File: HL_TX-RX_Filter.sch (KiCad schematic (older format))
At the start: 186 parts, among them J1 To Antenna, J2 From Tx, J3 ICSP, J4 Data In, J5 SCL SDA, J6 To Rx in, Q1 2N7002, Q2 2N7002, Q3 2N7002, Q4 2N7002, Q5 2N7002, Q6 2N7002, Q7 2N7002, Q8 2N7002, U1 LD1117S33TR, U10 PE4259, U11 PE4259, U12 PE4259, U13 PE4259, U2 ATMEGA328-AU, U3 PE4259, U4 PE4259, U5 PE4259, U6 PE4259, U7 PE4259, U8 PE4259, U9 PE4259

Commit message: Further progress on layout
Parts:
- added C69, C70, C71, C72: .1u, Capacitors_SMD:C_1206_HandSoldering, symbol C
- added J10: CNR4, Connectors:1pin, symbol TEST_1P
- added J7: CNR1, Connectors:1pin, symbol TEST_1P
- added J8: CNR3, Connectors:1pin, symbol TEST_1P
- added J9: CNR2, Connectors:1pin, symbol TEST_1P
- D13, D14: footprint Diodes_SMD:MELF_Handsoldering -> Diodes_SMD:D_MiniMELF_Handsoldering
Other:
- moved on the sheet: L11, L12, L13, L14

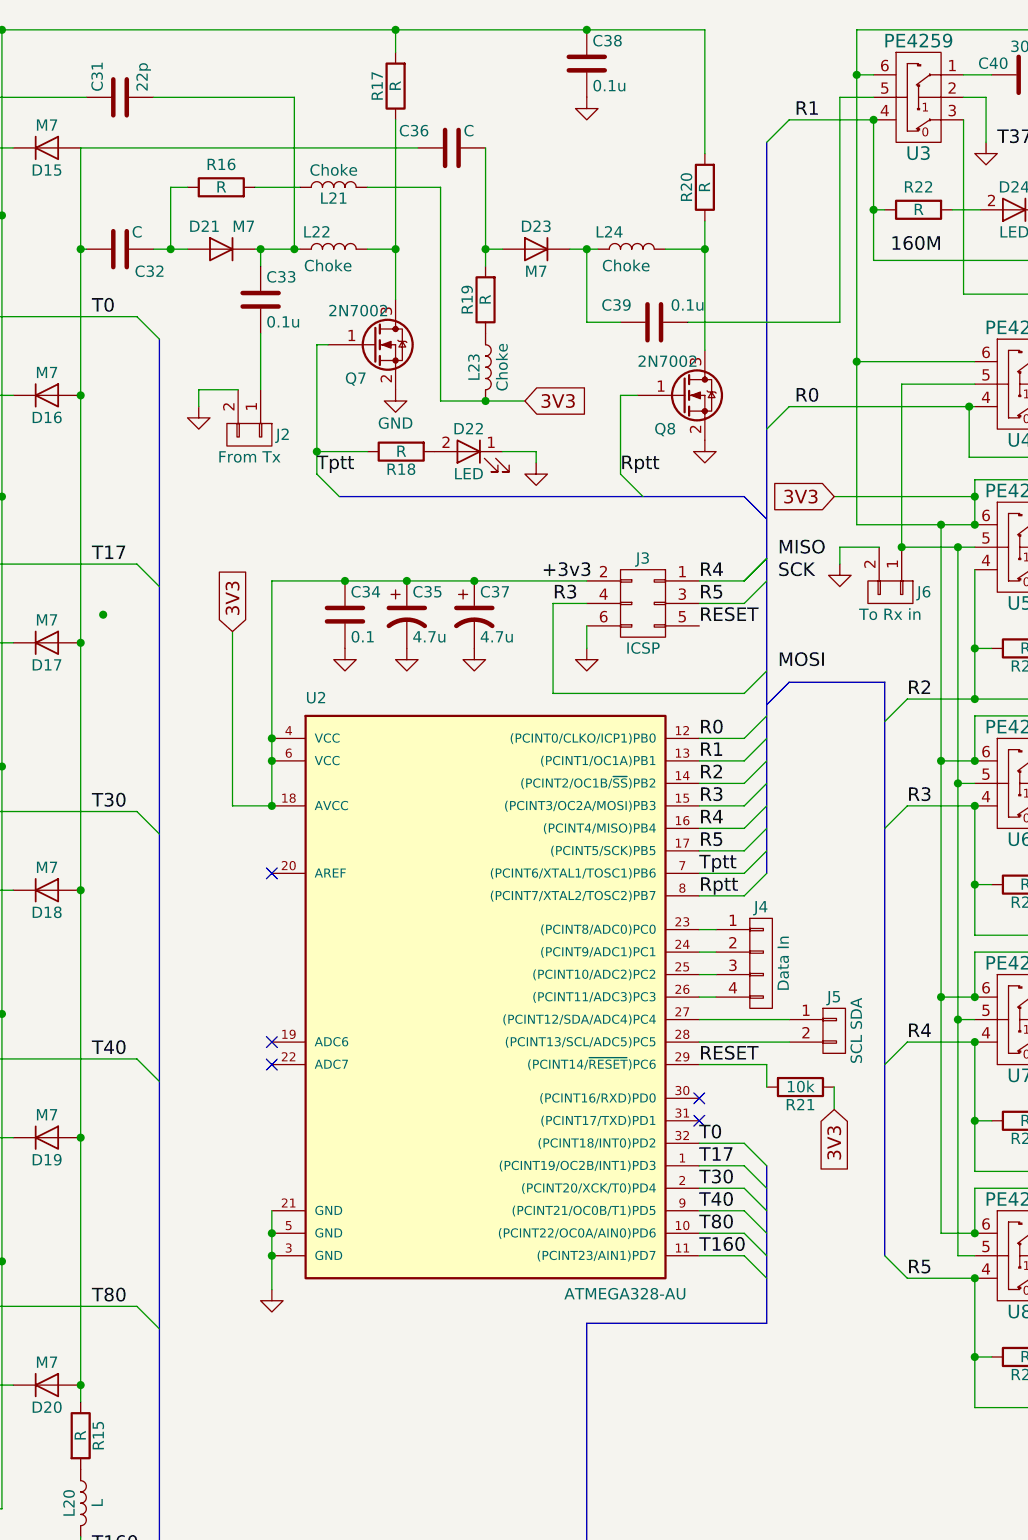
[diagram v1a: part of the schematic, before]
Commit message: Rearranging pins on microprocessor to better fit layout
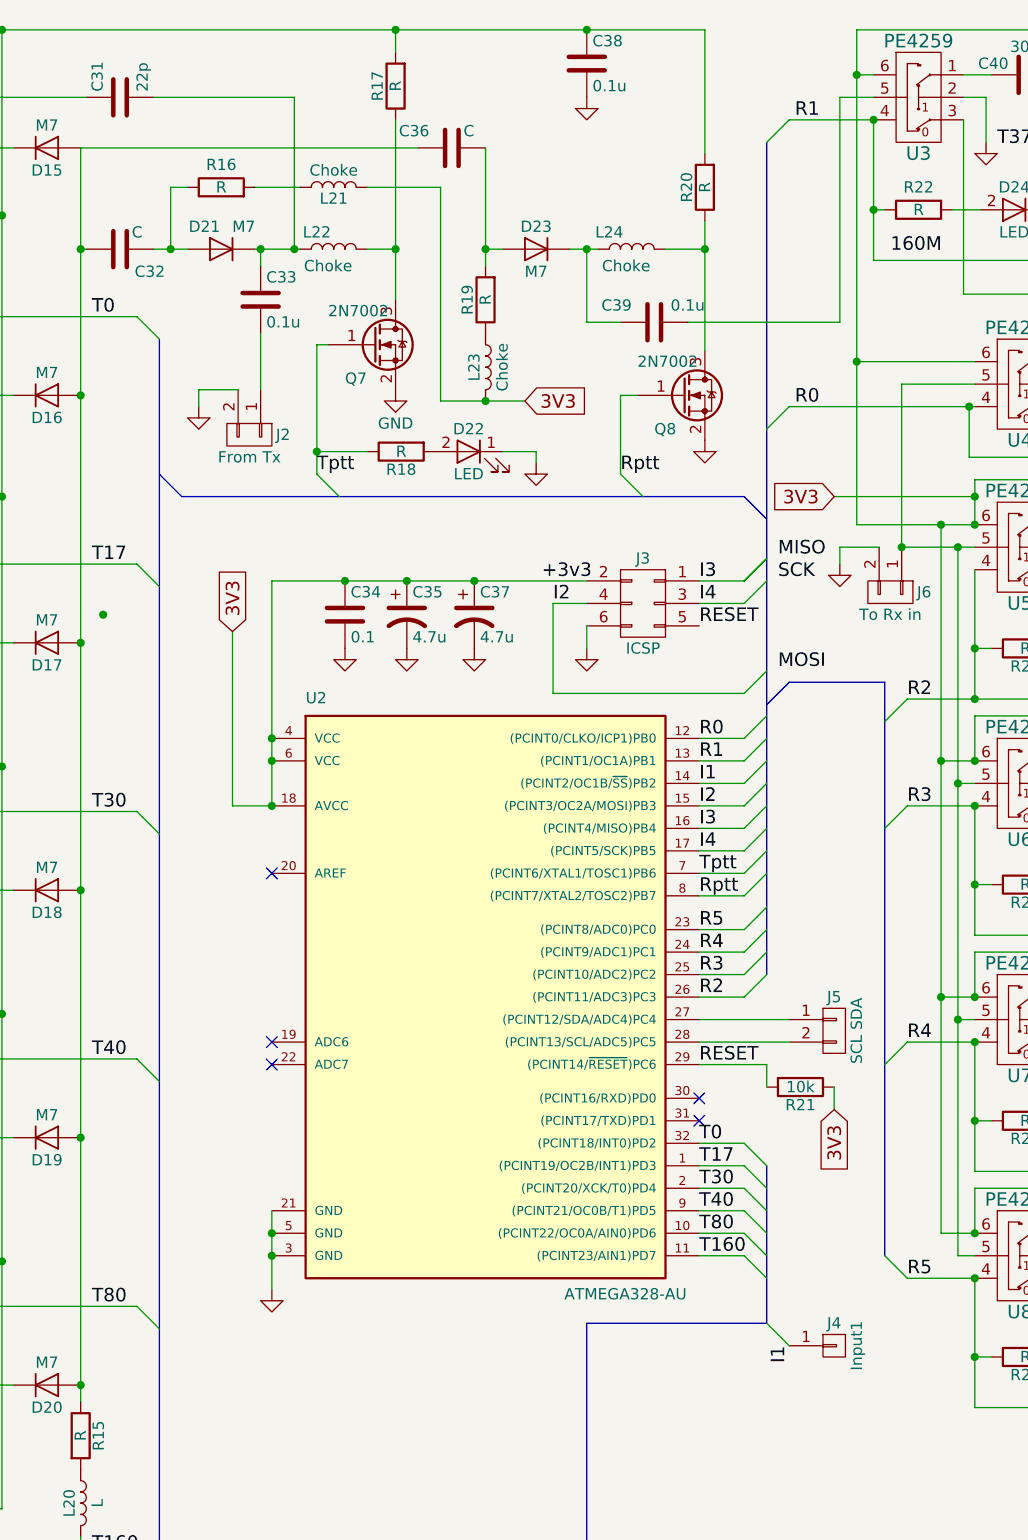
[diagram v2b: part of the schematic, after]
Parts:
- removed J4: Data In, Pin_Headers:Pin_Header_Straight_1x04, symbol CONN_01X04
- added J4: Input1, Pin_Headers:Pin_Header_Straight_1x01_Pitch2.54mm, symbol CONN_01X01
- J1, J2, J5, J6: footprint Pin_Headers:Pin_Header_Straight_1x02 -> Pin_Headers:Pin_Header_Straight_1x02_Pitch2.54mm
- J3: footprint Pin_Headers:Pin_Header_Straight_1x06 -> Pin_Headers:Pin_Header_Straight_2x03_Pitch2.54mm
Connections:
- net labels added: I1, I2, I3, I4
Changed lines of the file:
@@
 R1
 Text Label 7300 3950 0    60   ~ 0
-R2
-Text Label 7300 4050 0    60   ~ 0
+I1
+Text Label 7300 4800 0    60   ~ 0
 R3
 Text Label 7300 4150 0    60   ~ 0
-R4
+I3
 Text Label 7300 4250 0    60   ~ 0
-R5
+I4
 Entry Wire Line
 	7600 2375 7700 2275
@@
 F 0 "J3" H 7050 3350 50  0000 C CNN
 F 1 "ICSP" H 7050 2950 50  0000 C CNN
-F 2 "Pin_Headers:Pin_Header_Straight_1x06" H 7050 1950 50  0001 C CNN
+F 2 "Pin_Headers:Pin_Header_Straight_2x03_Pitch2.54mm" H 7050 1950 50  0001 C CNN
 F 3 "" H 7050 1950 50  0001 C CNN
 	1    7050 3150
@@
 	7500 3150 7600 3050
 Text Label 7300 3050 0    60   ~ 0
-R4
+I3
 Text Label 7300 3150 0    60   ~ 0
-R5
+I4
 Text Label 7650 2950 0    60   ~ 0
 MISO
@@
 	7500 3550 7600 3450
 Text Label 6650 3150 0    60   ~ 0
-R3
+I2
 $Comp
 L GND #PWR054
@@
 F 0 "J1" V 1075 2275 50  0000 C CNN
 F 1 "To Antenna" V 1175 2125 50  0000 C CNN
-F 2 "Pin_Headers:Pin_Header_Straight_1x02" H 1075 2125 50  0001 C CNN
+F 2 "Pin_Headers:Pin_Header_Straight_1x02_Pitch2.54mm" H 1075 2125 50  0001 C CNN
 F 3 "" H 1075 2125 50  0001 C CNN
 	1    1075 2125
@@
 F 0 "J2" V 5300 2550 50  0000 C CNN
 F 1 "From Tx" V 5400 2400 50  0000 C CNN
-F 2 "Pin_Headers:Pin_Header_Straight_1x02" H 5300 2400 50  0001 C CNN
+F 2 "Pin_Headers:Pin_Header_Straight_1x02_Pitch2.54mm" H 5300 2400 50  0001 C CNN
 F 3 "" H 5300 2400 50  0001 C CNN
 	1    5300 2400
@@
 F 0 "J6" V 8150 3250 50  0000 C CNN
 F 1 "To Rx in" V 8250 3100 50  0000 C CNN
-F 2 "Pin_Headers:Pin_Header_Straight_1x02" H 8150 3100 50  0001 C CNN
+F 2 "Pin_Headers:Pin_Header_Straight_1x02_Pitch2.54mm" H 8150 3100 50  0001 C CNN
 F 3 "" H 8150 3100 50  0001 C CNN
 	1    8150 3100
@@
 	8075 1000 7700 1000
 Wire Bus Line
-	7600 1100 7600 4350
+	7600 1100 7600 4800
 Wire Wire Line
 	7300 3750 7500 3750
@@
 	2900 900  3125 900
 Wire Bus Line
-	5700 2675 7500 2675
+	5000 2675 7500 2675
 Wire Wire Line
 	7900 5400 7900 5300
@@
 F 0 "J5" H 7900 5200 50  0000 C CNN
 F 1 "SCL SDA" V 8000 5050 50  0000 C CNN
-F 2 "Pin_Headers:Pin_Header_Straight_1x02" H 7900 5050 50  0001 C CNN
+F 2 "Pin_Headers:Pin_Header_Straight_1x02_Pitch2.54mm" H 7900 5050 50  0001 C CNN
 F 3 "" H 7900 5050 50  0001 C CNN
 	1    7900 5050
@@
 Wire Wire Line
 	7300 5100 7700 5100
-$Comp
-L CONN_01X04 J4
-U 1 1 596806D9
-P 7575 4750
-F 0 "J4" H 7575 5000 50  0000 C CNN
-F 1 "Data In" V 7675 4750 50  0000 C CNN
-F 2 "Pin_Headers:Pin_Header_Straight_1x04" H 7575 4750 50  0001 C CNN
-F 3 "" H 7575 4750 50  0001 C CNN
-	1    7575 4750
-	1    0    0    -1
-$EndComp
-Wire Wire Line
-	7300 4600 7375 4600
-Wire Wire Line
-	7300 4700 7375 4700
-Wire Wire Line
-	7300 4800 7375 4800
-Wire Wire Line
-	7300 4900 7375 4900
+Wire Wire Line
+	7300 4600 7500 4600
+Wire Wire Line
+	7300 4700 7500 4700
+Wire Wire Line
+	7300 4800 7500 4800
+Wire Wire Line
+	7300 4900 7500 4900
 Wire Wire Line
 	7600 5200 7600 5300
@@
 Connection ~ 3250 6925
 Connection ~ 3300 6925
+Entry Bus Bus
+	4900 2575 5000 2675
+Entry Wire Line
+	7500 4900 7600 4800
+Entry Wire Line
+	7500 4800 7600 4700
+Entry Wire Line
+	7500 4700 7600 4600
+Entry Wire Line
+	7500 4600 7600 4500
+Text Label 7300 4600 0    60   ~ 0
+R5
+Text Label 7300 4700 0    60   ~ 0
+R4
+Text Label 7300 4050 0    60   ~ 0
+I2
+Text Label 7300 4900 0    60   ~ 0
+R2
+$Comp
+L CONN_01X01 J4
+U 1 1 59718308
+P 7900 6450
+F 0 "J4" H 7900 6550 50  0000 C CNN
+F 1 "Input1" V 8000 6450 50  0000 C CNN
+F 2 "Pin_Headers:Pin_Header_Straight_1x01_Pitch2.54mm" H 7900 6450 50  0001 C CNN
+F 3 "" H 7900 6450 50  0001 C CNN
+	1    7900 6450
+	1    0    0    -1
+$EndComp
+Entry Wire Line
+	7600 6350 7700 6450
+Text Label 7700 6450 3    60   ~ 0
+I1
 $EndSCHEMATC

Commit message: Re-annotated board
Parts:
- removed U1: LD1117S33TR, TO_SOT_Packages_SMD:SOT-223, symbol LD1117S33TR
- added R1, R18, R2, R20, R21, R3: R, Resistors_SMD:R_1206_HandSoldering, symbol R
- U10: renamed from U11; footprint TO_SOT_Packages_SMD:SC-70-6 -> TO_SOT_Packages_SMD:SOT-363_SC-70-6_Handsoldering
- U11: renamed from U12; footprint TO_SOT_Packages_SMD:SC-70-6 -> TO_SOT_Packages_SMD:SOT-363_SC-70-6_Handsoldering
- U12: renamed from U13; footprint TO_SOT_Packages_SMD:SC-70-6 -> TO_SOT_Packages_SMD:SOT-363_SC-70-6_Handsoldering
- U2: renamed from U3; footprint TO_SOT_Packages_SMD:SC-70-6 -> TO_SOT_Packages_SMD:SOT-363_SC-70-6_Handsoldering
- U3: renamed from U4; footprint TO_SOT_Packages_SMD:SC-70-6 -> TO_SOT_Packages_SMD:SOT-363_SC-70-6_Handsoldering
- U4: renamed from U5; footprint TO_SOT_Packages_SMD:SC-70-6 -> TO_SOT_Packages_SMD:SOT-363_SC-70-6_Handsoldering
- U5: renamed from U6; footprint TO_SOT_Packages_SMD:SC-70-6 -> TO_SOT_Packages_SMD:SOT-363_SC-70-6_Handsoldering
- U6: renamed from U7; footprint TO_SOT_Packages_SMD:SC-70-6 -> TO_SOT_Packages_SMD:SOT-363_SC-70-6_Handsoldering
- U7: renamed from U8; footprint TO_SOT_Packages_SMD:SC-70-6 -> TO_SOT_Packages_SMD:SOT-363_SC-70-6_Handsoldering
- U8: renamed from U9; footprint TO_SOT_Packages_SMD:SC-70-6 -> TO_SOT_Packages_SMD:SOT-363_SC-70-6_Handsoldering
- U9: renamed from U10; footprint TO_SOT_Packages_SMD:SC-70-6 -> TO_SOT_Packages_SMD:SOT-363_SC-70-6_Handsoldering
- renumbered C67 to C16, C68 to C17, C69 to C18, C70 to C19, C71 to C20, C72 to C21, C17 to C22, C18 to C23, C19 to C24, C20 to C25, C16 to C26, C21 to C27, C22 to C28, C23 to C29, C24 to C30, C25 to C31, C26 to C32, C27 to C33, C28 to C34, C29 to C35, C30 to C36, C31 to C37, C32 to C38, C33 to C39, C34 to C40, C35 to C41, C36 to C42, C37 to C43, C38 to C44, C39 to C45, C40 to C46, C41 to C47, C42 to C48, C43 to C49, C44 to C50, C45 to C51, C46 to C52, C47 to C53, C48 to C54, C49 to C55, C50 to C56, C51 to C57, C52 to C58, C53 to C59, C54 to C60, C55 to C61, C56 to C62, C57 to C63, C58 to C64, C59 to C65, C60 to C66, C61 to C67, C62 to C68, C63 to C69, C64 to C70, C65 to C71, C66 to C72, J7 to J1, J6 to J10, J8 to J2, J9 to J3, J10 to J4, J1 to J5, J2 to J6, J3 to J7, J5 to J8, J4 to J9, R7 to R10, R8 to R11, R9 to R12, R10 to R13, R11 to R14, R12 to R15, R13 to R16, R14 to R17, R15 to R19, R16 to R22, R17 to R23, R18 to R24, R19 to R25, R20 to R26, R21 to R27, R22 to R28, R23 to R29, R24 to R30, R25 to R31, R26 to R32, R27 to R33, R1 to R4, R2 to R5, R3 to R6, R4 to R7, R5 to R8, R6 to R9, U2 to U1
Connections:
- wire segments 351 -> 354
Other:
- moved on the sheet: L20, L3, R19

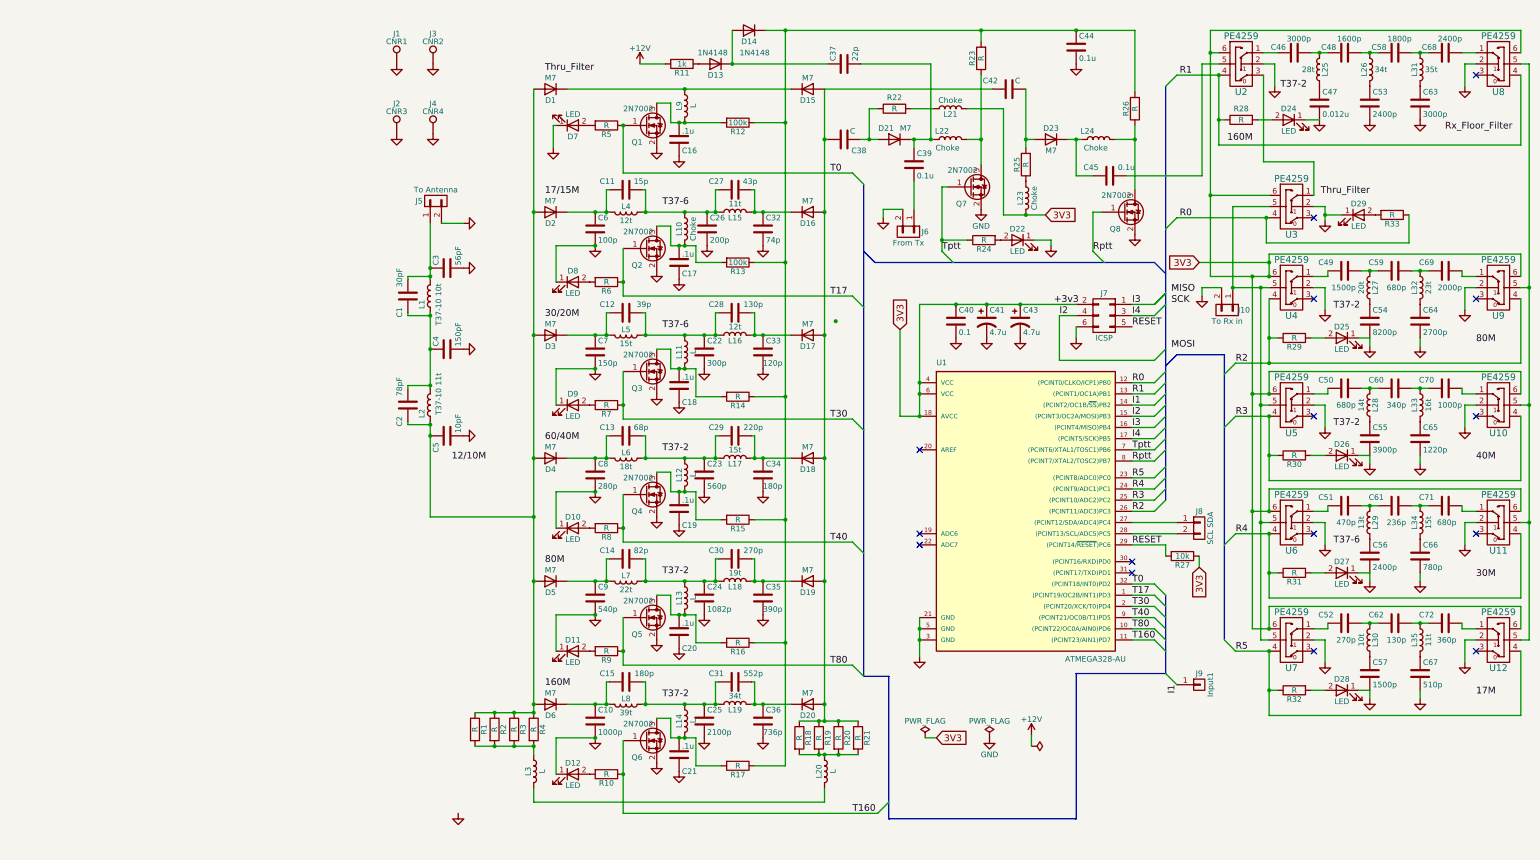
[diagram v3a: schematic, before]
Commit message: Re-building PCB after annotation redo
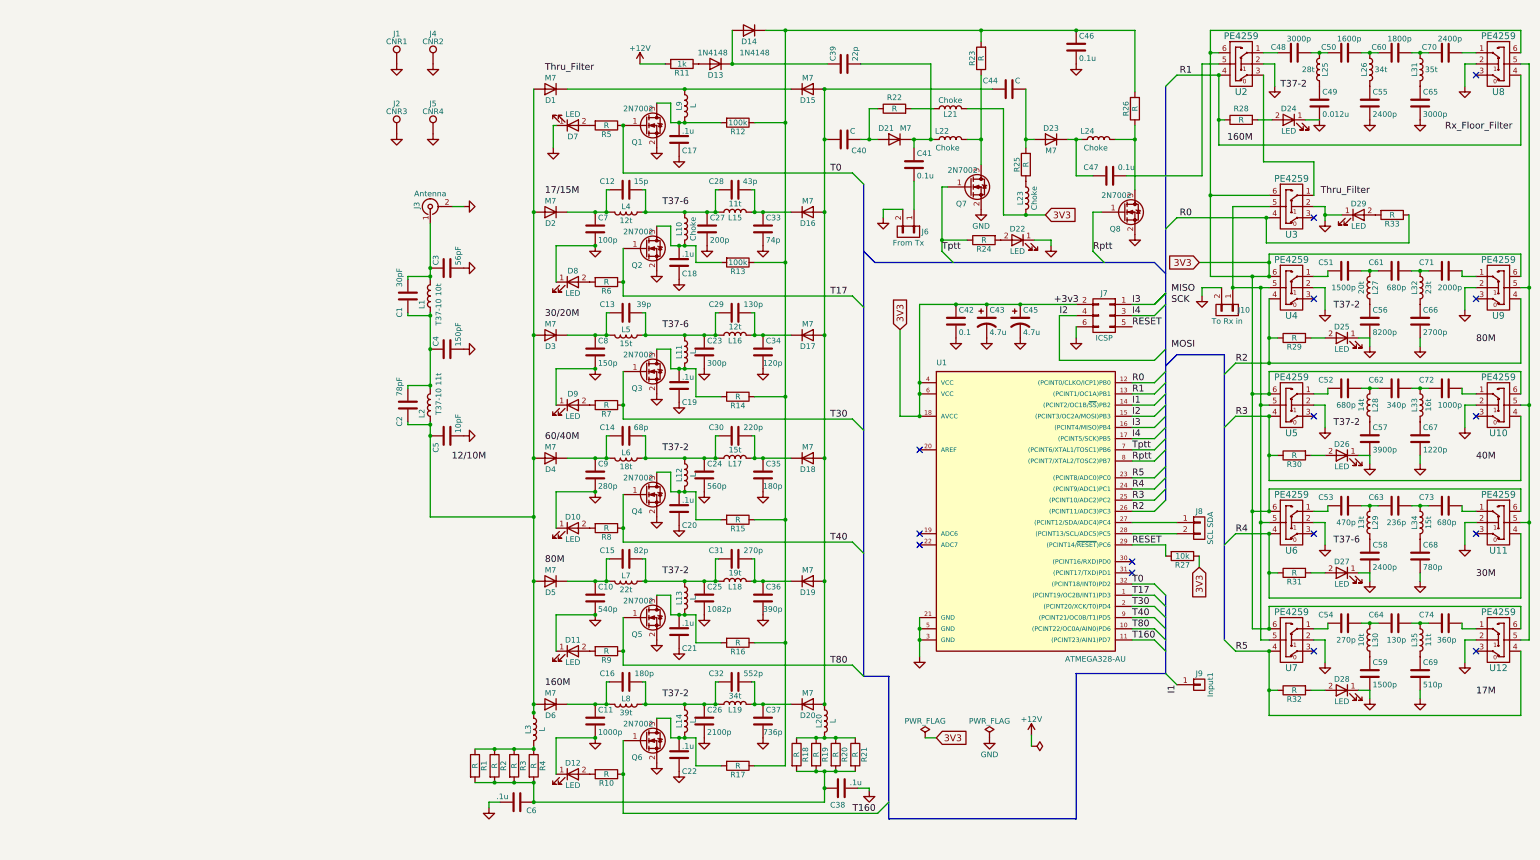
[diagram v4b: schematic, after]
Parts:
- removed J5: To Antenna, Pin_Headers:Pin_Header_Straight_1x02_Pitch2.54mm, symbol CONN_01X02
- added C38, C6: .1u, Capacitors_SMD:C_1206_HandSoldering, symbol C
- added J3: Antenna, Connectors_G:SMAEDGE_TH, symbol CONN_COAXIAL
- renumbered C9 to C10, C10 to C11, C11 to C12, C12 to C13, C13 to C14, C14 to C15, C15 to C16, C16 to C17, C17 to C18, C18 to C19, C19 to C20, C20 to C21, C21 to C22, C22 to C23, C23 to C24, C24 to C25, C25 to C26, C26 to C27, C27 to C28, C28 to C29, C29 to C30, C30 to C31, C31 to C32, C32 to C33, C33 to C34, C34 to C35, C35 to C36, C36 to C37, C37 to C39, C38 to C40, C39 to C41, C40 to C42, C41 to C43, C42 to C44, C43 to C45, C44 to C46, C45 to C47, C46 to C48, C47 to C49, C48 to C50, C49 to C51, C50 to C52, C51 to C53, C52 to C54, C53 to C55, C54 to C56, C55 to C57, C56 to C58, C57 to C59, C58 to C60, C59 to C61, C60 to C62, C61 to C63, C62 to C64, C63 to C65, C64 to C66, C65 to C67, C66 to C68, C67 to C69, C6 to C7, C68 to C70, C69 to C71, C70 to C72, C71 to C73, C72 to C74, C7 to C8, C8 to C9, J3 to J4, J4 to J5
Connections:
- net GND: now also C38.1, C6.1, J3.2 (Ext)
- net at C40.1, C44.1, D15.2 (A)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: now also L20.1; no longer R18.1, R19.1, R20.1, R21.1
- net at C2.1, C5.1, D1.2 (A)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: now also L3.1; no longer R1.1, R2.1, R3.1, R4.1
- net at R1.2, R2.2, R3.2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: now also R18.2, R19.2, R20.2, R21.2, C38.2, C6.2; no longer L3.1
- net at L3.2: now also R1.1, R2.1, R3.1, R4.1; no longer L20.2
- net at C1.2, C3.1, L1.2: now also J3.1 (In)
- new net: L20.2, R18.1, R19.1, R20.1, R21.1
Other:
- moved on the sheet: L20, L3, R1, R18, R19, R2, R20, R21, R3, R4

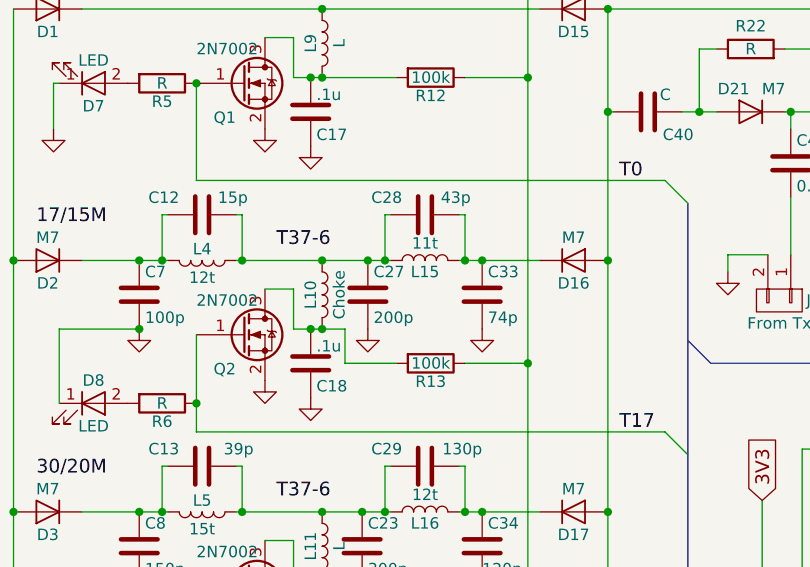
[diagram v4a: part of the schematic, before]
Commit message: Rearranging layout for re-annotated schematic
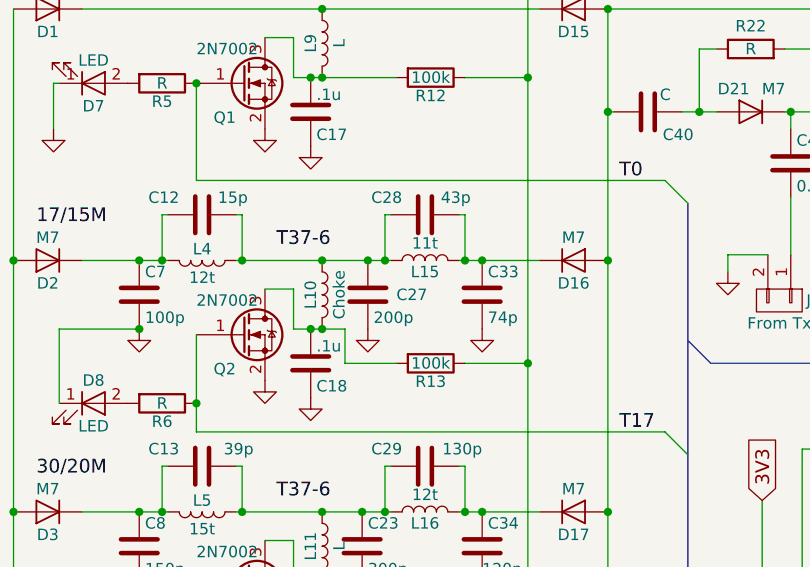
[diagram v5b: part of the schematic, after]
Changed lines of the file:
@@
 U 1 1 58EF6AB2
 P 3500 2375
-F 0 "C27" H 3525 2475 50  0000 L CNN
+F 0 "C27" H 3625 2375 50  0000 L CNN
 F 1 "200p" H 3525 2275 50  0000 L CNN
 F 2 "Capacitors_SMD:C_1206_HandSoldering" H 3538 2225 50  0001 C CNN
